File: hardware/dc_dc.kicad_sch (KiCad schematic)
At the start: 3 parts, among them IC3 XCL240B333FR-G

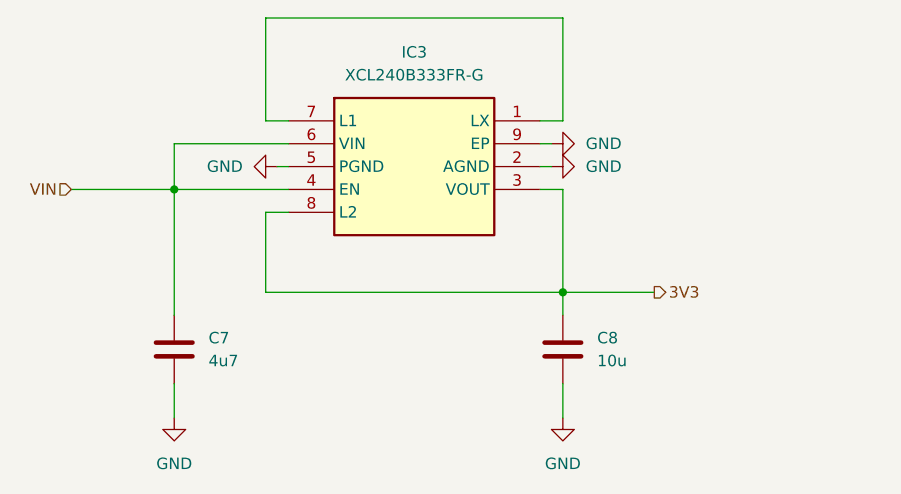
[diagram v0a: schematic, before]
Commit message: Battery temperature meter added to MCU
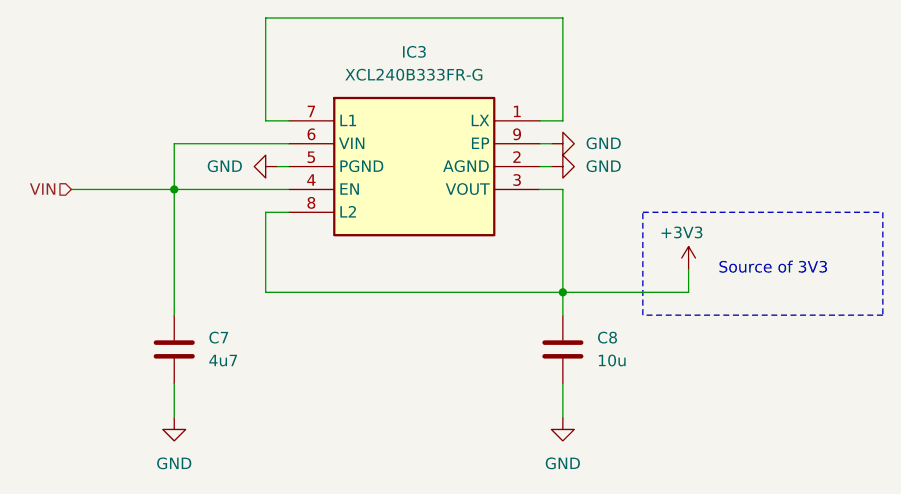
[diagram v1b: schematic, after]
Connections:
- net 3V3 renamed +3V3
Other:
- note added: "Source of 3V3"
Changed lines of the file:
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@@
 	(wire
 		(pts
-			(xy 124.46 91.44) (xy 134.62 91.44)
+			(xy 124.46 91.44) (xy 138.43 91.44)
 		)
 		(stroke
@@
 	(wire
 		(pts
+			(xy 138.43 88.9) (xy 138.43 91.44)
+		)
+		(stroke
+			(width 0)
+			(type default)
+		)
+	)
+	(wire
+		(pts
 			(xy 91.44 72.39) (xy 93.98 72.39)
 		)
@@
 			(width 0)
 			(type default)
+		)
+	)
+	(rectangle
+		(start 133.35 82.55)
+		(end 160.02 93.98)
+		(stroke
+			(width 0)
+			(type dot)
+		)
+		(fill
+			(type none)
+		)
+	)
+	(text "Source of 3V3"
+		(exclude_from_sim no)
+		(at 141.732 88.9 0)
+		(effects
+			(font
+				(size 1.27 1.27)
+			)
+			(justify left)
 		)
 	)
@@
 			)
 			(justify right)
-		)
-	)
-	(hierarchical_label "3V3"
-		(shape output)
-		(at 134.62 91.44 0)
-		(effects
-			(font
-				(size 1.27 1.27)
-			)
-			(justify left)
 		)
 	)
@@
 					(unit 1)
 				)
+			)
+		)
+	)
+	(symbol
+		(lib_id "power:+3V3")
+		(at 138.43 88.9 0)
+		(unit 1)
+		(exclude_from_sim no)
+		(in_bom yes)
+		(on_board yes)
+		(dnp no)
+		(property "Reference" "#PWR067"
+			(at 138.43 92.71 0)
+			(effects
+				(font
+					(size 1.27 1.27)
+				)
+				(hide yes)
+			)
+		)
+		(property "Value" "+3V3"
+			(at 137.668 84.836 0)
+			(effects
+				(font
+					(size 1.27 1.27)
+				)
+			)
+		)
+		(property "Footprint" ""
+			(at 138.43 88.9 0)
+			(effects
+				(font
+					(size 1.27 1.27)
+				)
+				(hide yes)
+			)
+		)
+		(property "Datasheet" ""
+			(at 138.43 88.9 0)
+			(effects
+				(font
+					(size 1.27 1.27)
+				)
+				(hide yes)
+			)
+		)
+		(property "Description" "Power symbol creates a global label with name \"+3V3\""
+			(at 138.43 88.9 0)
+			(effects
+				(font
+					(size 1.27 1.27)
+				)
+				(hide yes)
+			)
+		)
+		(pin "1"
+		)
+		(instances
+			(project "obvod"
+				(path "/e8e834c4-1afb-42f7-b718-3cb720dae1d5/c10e3bb1-4b24-45b1-b428-aefa65422361"
+					(reference "#PWR067")
+					(unit 1)
+				)

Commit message: Revised and completed BOM
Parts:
- C7, C8: footprint (none) -> Capacitor_SMD:C_0805_2012Metric
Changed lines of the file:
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@@
 			)
 		)
-		(property "Footprint" ""
+		(property "Footprint" "Capacitor_SMD:C_0805_2012Metric"
 			(at 82.2452 101.6 0)
 			(effects
@@
 			)
 		)
-		(property "Footprint" ""
+		(property "Footprint" "Capacitor_SMD:C_0805_2012Metric"
 			(at 125.4252 101.6 0)
 			(effects
